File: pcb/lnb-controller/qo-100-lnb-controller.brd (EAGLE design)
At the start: 60 x 75 mm, 71 parts, among them CON1 2EDG-2P, Q1 AO3401, U1 LT8636, U2 ADP7142AUJZ-3.3, U3 DSC1201DE3-25M00000, U4 DSB321SDA, U5 MXT573ABC25M0000

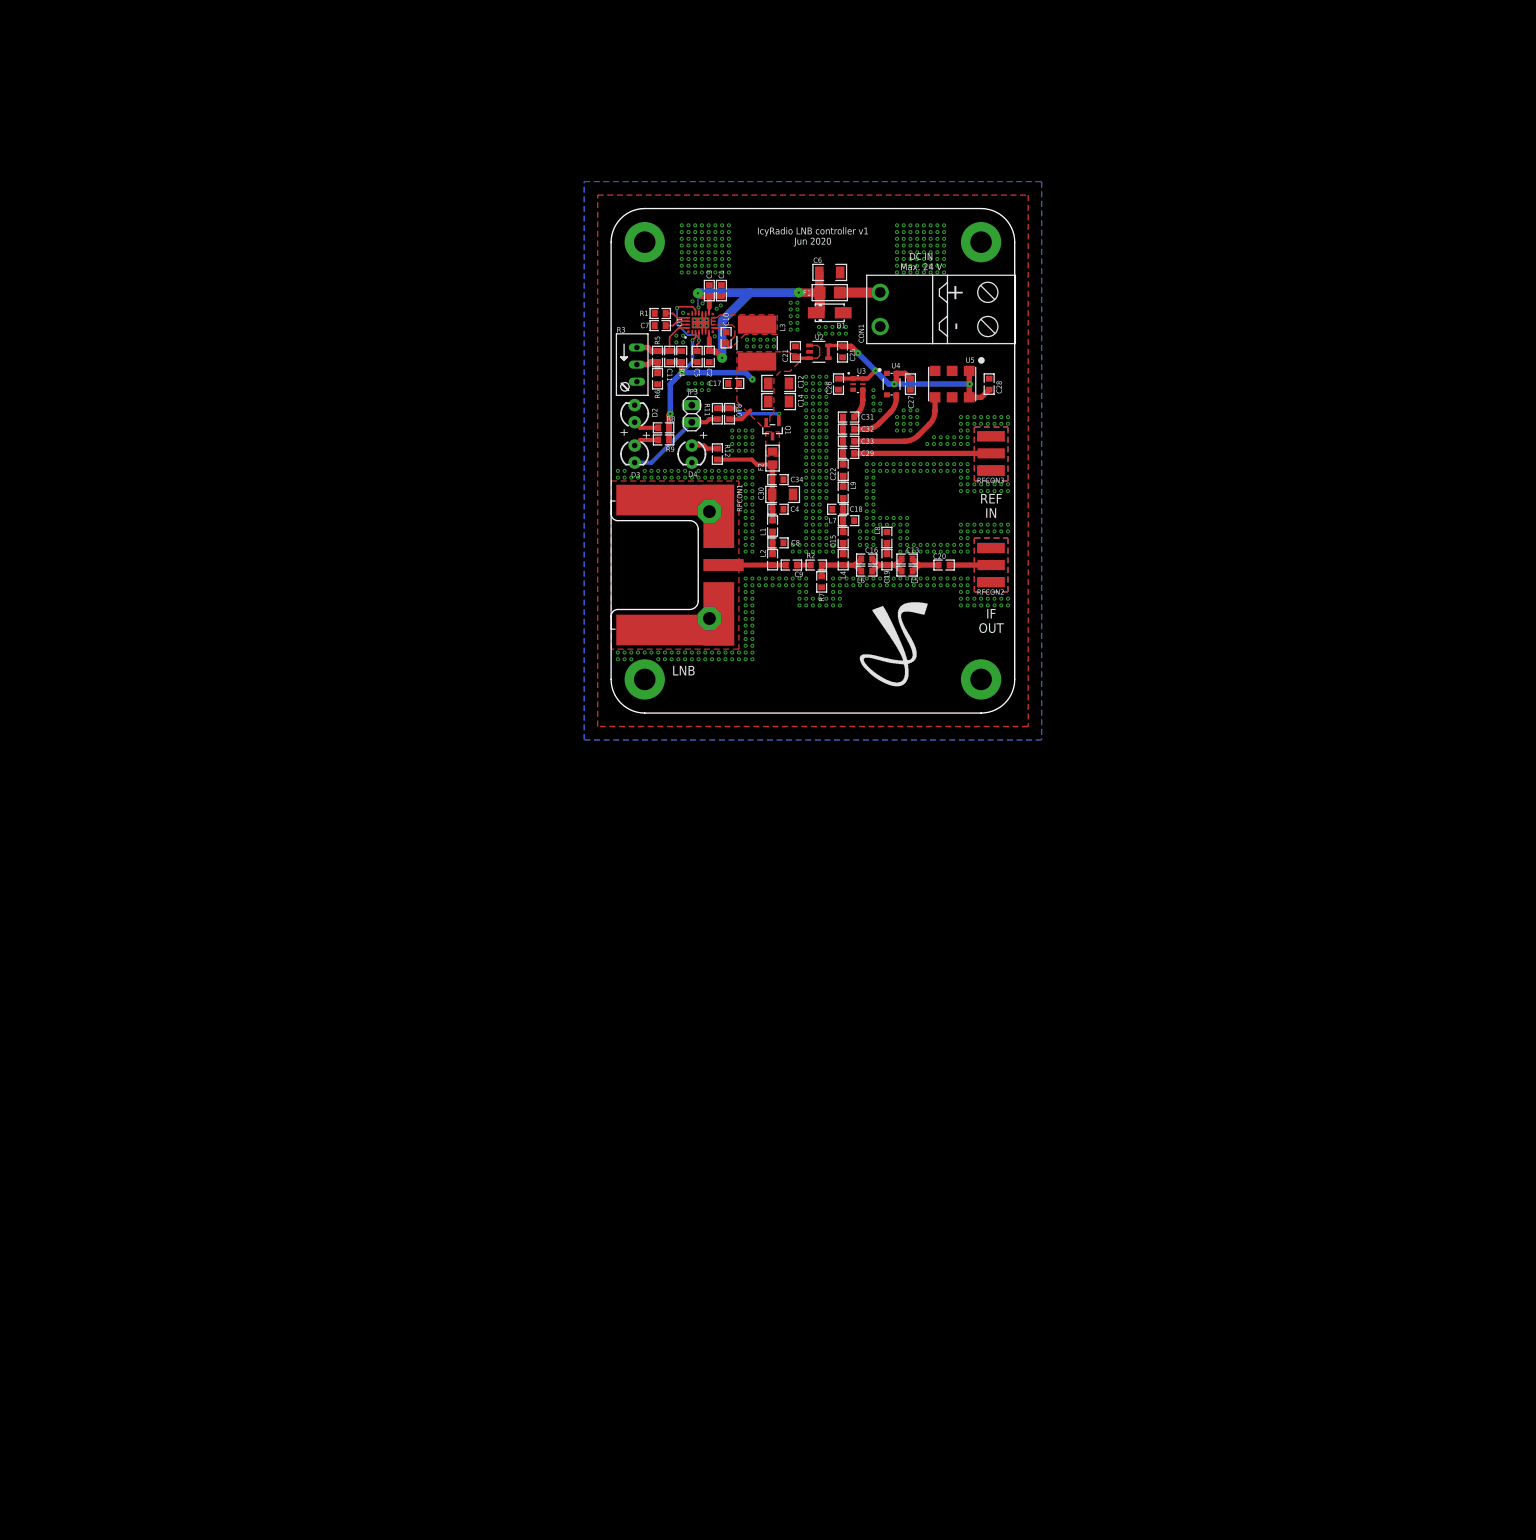
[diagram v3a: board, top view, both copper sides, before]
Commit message: Re-design LNB controller
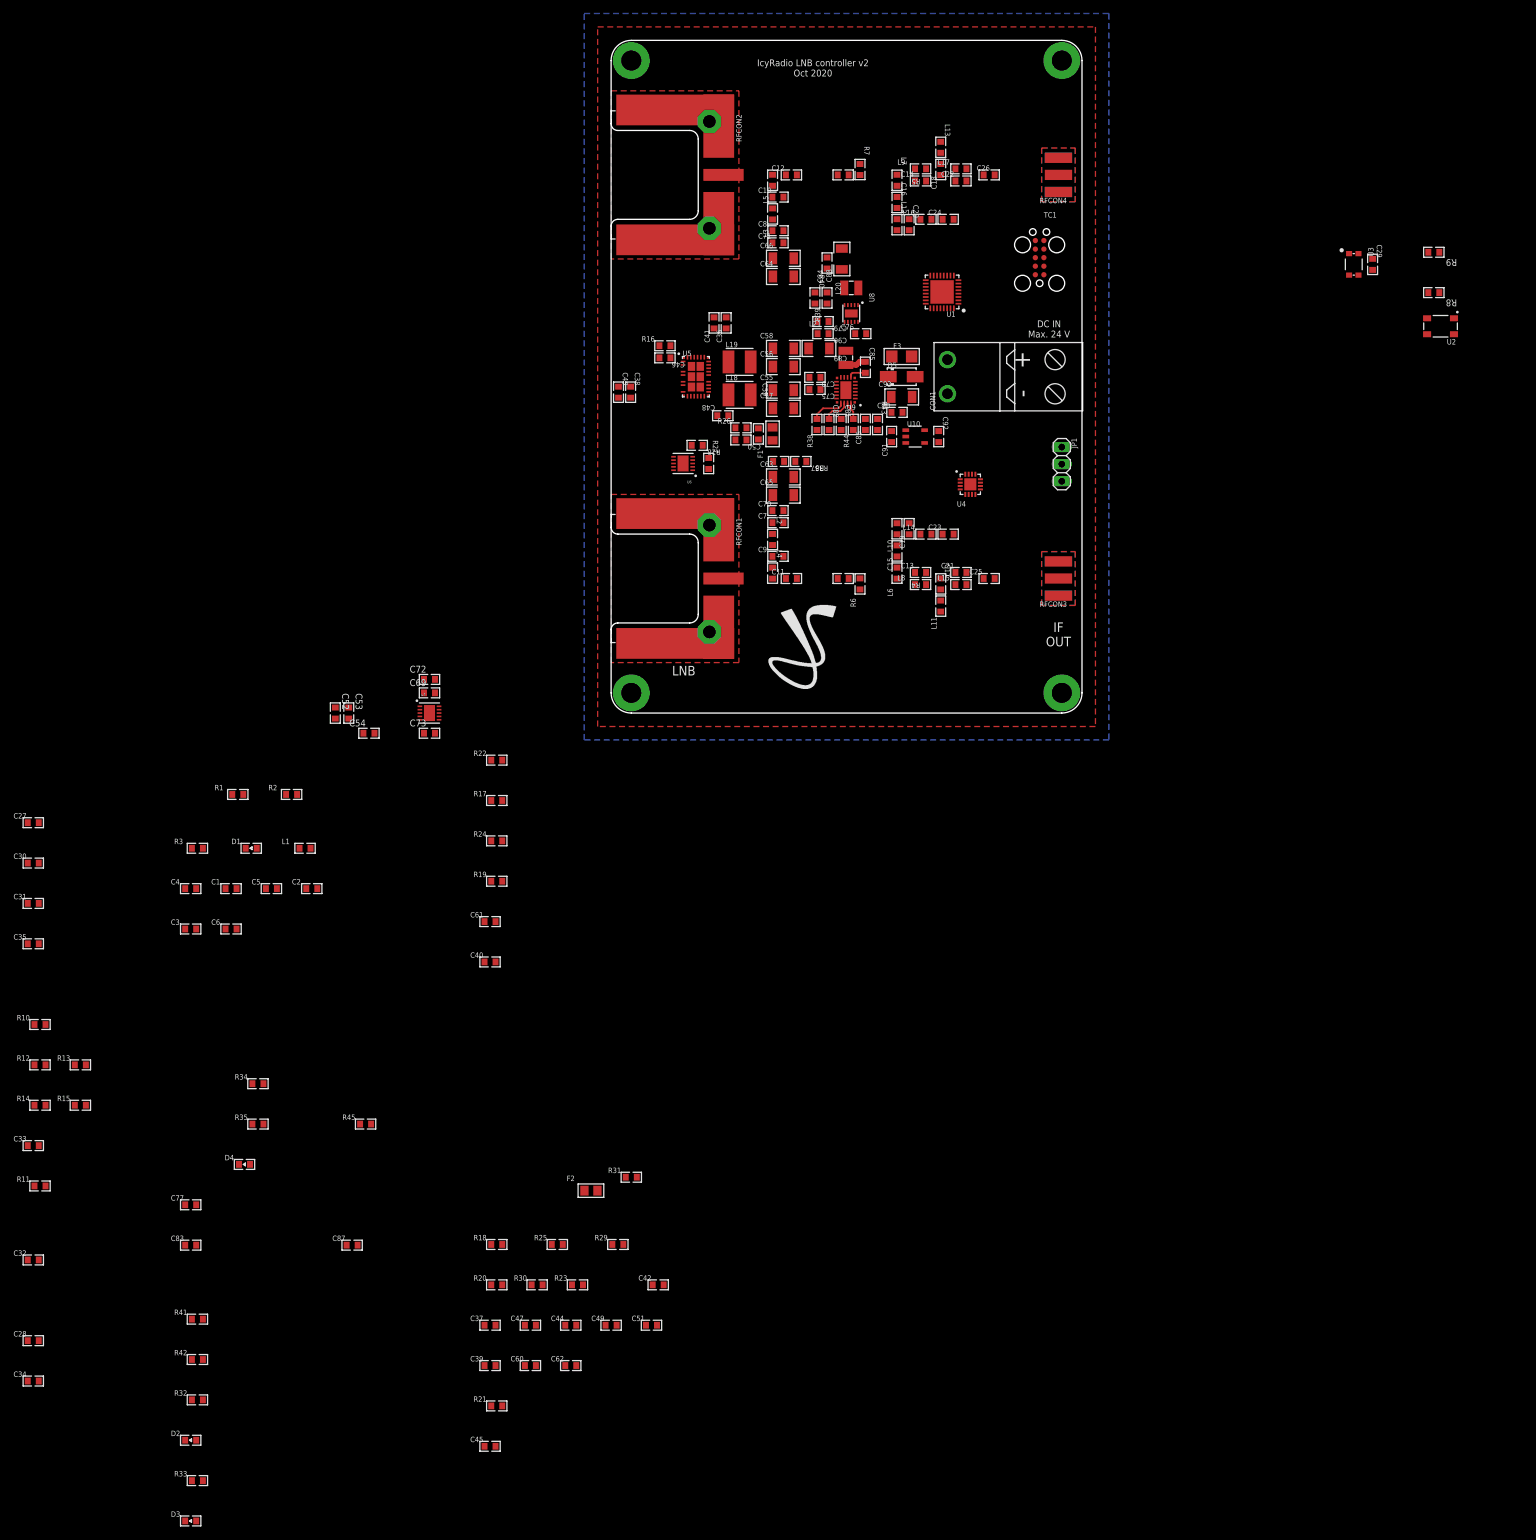
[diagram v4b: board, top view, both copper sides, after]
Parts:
- removed JP3: PINHD-1X2, Pin Header:1X02
- removed Q1: AO3401, Alpha Omega:SOT23
- added C23, C24: 100pF, Capacitor:CAP0603
- added C35, C48, C49, C53, C59, C60, C61, C62, C70, C71, C72, C84, C85, C90: 100nF, Capacitor:CAP0603
- added C36, C37, C75, C76: 4.7uF, Capacitor:CAP0603
- added C38, C39, C40, C41, C42, C54, C73, C78, C80, C81, C91: 1uF, Capacitor:CAP0603
- added C43, C44: DNP, Capacitor:CAP0603
- added C45, C77, C79, C83, C87: 470pF, Capacitor:CAP0603
- added C46, C47, C82: 10nF, Capacitor:CAP0603
- added C50, C51: 4.7pF, Capacitor:CAP0603
- added C52, C69, C92: 10uF, Capacitor:CAP0603
- added C55, C56, C57, C58, C63, C64, C65, C66: 22uF, Capacitor:CAP1206
- added C86: 10pF, Capacitor:CAP0603
- added C88, C89: 100uF, Capacitor:CAP1206
- added C93: 10uF, Capacitor:CAP1206
- added D5: SMAJ24A, TVS:DO214AC
- added F3: 2.6A Hold, PTC Fuses:1206
- added JP1: PINHD-1X3, Pin Header:1X03
- added L10, L12: 43nH, Inductor:IND0603
- added L11, L13: 330nH, Inductor:IND0603
- added L14, L16: 470nH, Inductor:IND0603
- added L15, L17: 120nH, Inductor:IND0603
- added L18, L19: 4.7uH, Inductor:IND0404
- added L20: 2.2uH, Inductor:IND2520
- added L21: 4.7uH, Inductor:IND2520
- added R13, R14, R15, R19, R20: 0 Ohms, Resistor:RES0603
- added R16: 15K Ohms, Resistor:RES0603
- added R17, R18, R24, R25, R34: 100K Ohms, Resistor:RES0603
- added R21: 1K Ohms, Resistor:RES0603
- added R22, R23, R27, R30: DNP, Resistor:RES0603
- added R26, R29, R43: 1M Ohms, Resistor:RES0603
- added R28, R31: 40.2K Ohms, Resistor:RES0603
- added R32, R33: 2.5K Ohms, Resistor:RES0603
- added R35: 10K Ohms, Resistor:RES0603
- added R36, R41: 90.9K Ohms, Resistor:RES0603
- added R37, R42: 12K Ohms, Resistor:RES0603
- added R38: 41.2K Ohms, Resistor:RES0603
- added R39: 309K Ohms, Resistor:RES0603
- added R40: 71.5K Ohms, Resistor:RES0603
- added R44: 226K Ohms, Resistor:RES0603
- added R45: 510 Ohms, Resistor:RES0603
- added RFCON4: RFCON-SMA-EDGE, RF Connector:SMA-EDGE
- added TC1: TC2050-IDC, TagConnect:TC2050-IDC
- added U10: ADP7142AUJZ-3.3, Analog Devices:SOT23-5
- added U6, U7: AD5272-100, Analog Devices:DFN10
- added U8: MIC23155, Microchip:DFN10
- added U9: LT8636, Analog Devices:QFN20_ASYM_CORNER
- C1: value 4.7uF -> 100nF
- C10, C17, C9: value 100nF -> 100pF
- C11: value 10pF -> 100nF
- C12, C30: value 22uF -> 100nF; device Capacitor:CAP1206 -> Capacitor:CAP0603
- C14: value 22uF -> 330pF; device Capacitor:CAP1206 -> Capacitor:CAP0603
- C16: value 330pF -> 100pF
- C18: value 1nF -> 100pF
- C19: value 100pF -> 1nF
- C2, C3: value 1uF -> 100nF
- C20: value 68pF -> 1nF
- C21: value 1uF -> 330pF
- C22: value 100pF -> 330pF
- C25: value 10uF -> 68pF
- C26: value 100nF -> 68pF
- C29, C31: value DNP -> 100nF
- C32: value DNP -> 15pF
- C33, C34: value 100nF -> 10pF
- C4: value 100nF -> 4.7uF
- C6: value 10uF -> 100nF; device Capacitor:CAP1206 -> Capacitor:CAP0603
- C7: value 10nF -> 100nF
- D1: value SMAJ24A -> LED0603; device TVS:DO214AC -> LED:0603
- D2, D3, D4: value LEDTH3MM -> LED0603; device LED:LED_3MM -> LED:0603
- F1: value 2.6A Hold -> (none); device PTC Fuses:1206 -> PTC Fuses:0805
- L1: value 470nH -> 4.7uH
- L3: value 4.7uH -> 470nH; device Inductor:IND0606 -> Inductor:IND0603
- L5, L6: value 120nH -> 470nH
- L7: value 43nH -> 470nH
- L8: value 330nH -> 120nH
- L9: value 470nH -> 120nH
- R1: value 41.2K Ohms -> 10K Ohms
- R10: value 10K Ohms -> 100K Ohms
- R12: value 2.5K Ohms -> 0 Ohms
- R2: value 43.2 Ohms -> 10K Ohms
- R3: value 100K Ohms -> 330 Ohms; device Potentiometer:TRIMMER -> Resistor:RES0603
- R4: value 1M Ohms -> 43.2 Ohms
- R5: value DNP -> 43.2 Ohms
- R6: value 47K Ohms -> 86.6 Ohms
- R8: value 2.5K Ohms -> 10K Ohms
- R9: value 2.5K Ohms -> 8.4K Ohms
- RFCON2: value RFCON-SMA-EDGE -> RFCON-F-EDGE; device RF Connector:SMA-EDGE -> RF Connector:F-EDGE
- U1: value LT8636 -> EFM32PG1B200F256GM32; device Analog Devices:QFN20_ASYM_CORNER -> EFM32:QFN32_0.5P_JPG
- U2: value ADP7142AUJZ-3.3 -> IQXT-210-3; device Analog Devices:SOT23-5 -> Crystal:IQXT-210-23
- U3: value DSC1201DE3-25M00000 -> DSB321SDA; device Microchip:VDFN6 -> Crystal:TCXO-3225
- U4: value DSB321SDA -> SI5351C-B-GM1; device Crystal:TCXO-3225 -> Silicon Labs:QFN16
- U5: value MXT573ABC25M0000 -> LT8650S-1; device Microchip:LGA6 -> Analog Devices:QFN28_ASYM_CORNER
- moved C28 201.0 mm to (-85.9, -93.3), turned to 0 degrees
- moved C34 173.8 mm to (-85.9, -99.3)
- moved C32 173.0 mm to (-85.9, -81.3), turned to 0 degrees
- moved D3 171.8 mm to (-62.5, -120.1), turned to 0 degrees
- moved D2 166.3 mm to (-62.5, -108.1), turned to 0 degrees
- moved C33 160.2 mm to (-85.9, -64.3), turned to 0 degrees
- moved R11 152.7 mm to (-84.9, -70.3), turned to 0 degrees
- moved C27 145.8 mm to (-85.9, -16.3), turned to 0 degrees
- moved C31 141.1 mm to (-85.9, -28.3), turned to 0 degrees
- moved R10 136.9 mm to (-84.9, -46.3), turned to 0 degrees
- moved R12 135.6 mm to (-84.9, -52.3), turned to 0 degrees
- moved C6 132.1 mm to (-56.5, -32.1)
- moved D4 124.8 mm to (-54.5, -67.1), turned to 0 degrees
- moved C30 124.1 mm to (-85.9, -22.3)
- moved C3 122.3 mm to (-62.5, -32.1), turned to 0 degrees
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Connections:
- removed net 12V0: C11.1, C12.1, C14.1, C17.1, C21.1, L3.2, Q1.2, R10.2, R4.2, R8.2, R9.2, U1.2, U2.1, U2.3
- removed net 12V0_BST: C10.2, U1.7
- removed net 12V0_FB: C11.2, R3.E, R4.1, R5.2, U1.19, U1.20
- removed net 12V0_INTVCC: C5.1, U1.15, U1.3
- removed net 12V0_RT: R1.2, U1.17
- removed net 12V0_SS: C7.1, U1.18
- removed net 12V0_SW: C10.1, L3.1, U1.10, U1.8, U1.9
- removed net LNB_BIAS: C30.1, C34.1, C4.1, F2.1, L1.1, R12.2
- removed net LNB_REF: C22.2, C29.2, C31.2, C32.2, C33.2
- removed net N$2: D3.K, JP3.1, R11.1
- removed net N$5: D3.A, R9.1
- new net !REF_SYNTH_OE: R10.1, U4.3
- new net !RESET: R1.1, TC1.10, U1.8
- new net 1V8: C4.1, L1.1, U1.28
- new net 3V1: R10.2
- new net 3V3_FB: R39.1, R40.2, U8.4
- new net 3V3_REF_CLEAN: C28.1, C29.1, C30.1, C31.1, C35.1, C92.1, R8.2, U10.4, U10.5, U2.4, U3.4, U4.11, U4.14, U4.8, U4.9
- new net 3V3_SOFTSTART: C79.1, U8.6
- new net 3V3_SW: L20.1, U8.1
- new net 5V0: C76.1, C86.1, C89.1, C90.1, C91.1, L21.2, R43.2, R45.2, U10.1, U10.3, U8.2, U8.8, U8.9, U9.2
- new net 5V0_BST: C85.2, U9.7
- new net 5V0_FB: C86.2, R43.1, R44.2, U9.19, U9.20
- new net 5V0_INTVCC: C81.1, U9.15, U9.3
- new net 5V0_RT: R38.2, U9.17
- new net 5V0_SS: C82.1, U9.18
- new net 5V0_SW: C85.1, L21.1, U9.10, U9.8, U9.9
- new net BIAS_REG_TEMP: C45.1, R21.1
- new net CLK_MNGR_CLK0: R12.2, U4.10
- new net CLK_MNGR_CLK1: R14.2, U4.7
- new net CLK_MNGR_CLK2: R13.2, U4.13
- new net CLK_MNGR_CLK3: R15.2, U4.12
- new net I2C_SCL: U4.4, U6.9, U7.9
- new net I2C_SDA: U4.5, U6.8, U7.8
- new net LED: R3.2, U1.31
- new net LNB_BIAS_SEL: C6.1, JP1.2, R2.2, U1.32
- new net N$23: D3.A, R33.1
- new net N$24: C12.1, L5.2, RFCON2.SIGNAL
- new net N$25: D1.A, R3.1
- new net N$26: C12.2, R5.2
- new net N$27: C10.1, L3.2, L5.1
- new net N$28: C24.1, L16.2
- new net N$29: C16.1, L7.2
- new net N$30: C16.2, C20.1, L12.1, L16.1
- new net N$31: C14.1, L7.1, L9.1, R5.1, R7.2
- new net N$32: C14.2, C18.1, C22.1, L17.1, L9.2
- new net N$33: C26.2, RFCON4.SIG
- new net N$34: C18.2, L13.2
- new net N$35: C22.2, C26.1, L17.2
- new net N$36: C34.2, U4.1
- new net N$37: C32.1, U2.3, U4.6
- new net N$39: C54.1, U6.5
- new net N$40: C73.1, U7.5
- new net REF1: C23.2, R12.1
- new net REF2: C24.2, R14.1
- new net REF_XO_VC: R8.1, R9.2, U2.1
- new net SWCLK: TC1.4, U1.1
- new net SWDIO: TC1.2, U1.2
- new net SWO: TC1.6, U1.3
- new net VBIAS1: C63.1, C65.1, C7.1, C70.1, F1.1, L2.1, R32.2, R36.2
- new net VBIAS1_BST: C48.2, U5.15
- new net VBIAS1_EN: R17.2, U5.9
- new net VBIAS1_FB: C50.2, R26.1, R27.2, U5.27, U6.2
- new net VBIAS1_FB_DIV: R27.1, R28.2, U6.3
- new net VBIAS1_PG: R24.1, U5.12
- new net VBIAS1_SS: C46.1, U5.26
- new net VBIAS1_SW: C48.1, L18.1, U5.16, U5.17
- new net VBIAS1_UNFUSED: C50.1, C55.1, C57.1, C59.1, C61.1, F1.2, L18.2, R26.2, U5.22
- new net VBIAS1_VC: R19.1, R22.2, U5.28
- new net VBIAS1_VSENSE: C83.1, R36.1, R37.2, U1.19
- new net VBIAS2: C64.1, C66.1, C71.1, C8.1, F2.1, L3.1, R33.2, R41.2
- new net VBIAS2_BST: C49.2, U5.20
- new net VBIAS2_EN: R18.2, U5.8
- new net VBIAS2_FB: C51.2, R29.1, R30.2, U5.24, U7.2
- new net VBIAS2_FB_DIV: R30.1, R31.2, U7.3
- new net VBIAS2_PG: R25.1, U5.11
- new net VBIAS2_SS: C47.1, U5.25
- new net VBIAS2_SW: C49.1, L19.1, U5.18, U5.19
- new net VBIAS2_UNFUSED: C51.1, C56.1, C58.1, C60.1, C62.1, F2.2, L19.2, R29.2
- new net VBIAS2_VC: R20.1, R23.2, U5.23
- new net VBIAS2_VSENSE: C87.1, R41.1, R42.2, U1.20
- new net VBIAS_VCC: C40.1, R19.2, R20.2, U5.13, U5.21
- new net VIN_VSENSE: C77.1, R34.1, R35.2, U1.21
- net 3V3: now also C1.1, C2.1, C3.1, C52.1, C53.1, C69.1, C72.1, C84.1, C88.1, JP1.1, L20.2, R1.2, R24.2, R25.2, R39.2, TC1.1, U1.22, U1.27, U1.30, U1.5, U4.16, U6.1, U6.10, U6.7, U7.1, U7.7, U8.3; no longer C25.1, C26.1, C28.1, U2.4, U2.5, U3.1, U3.6, U4.4, U5.1, U5.6
- net GND: now also C10.2, C19.2, C20.2, C29.2, C31.2, C32.2, C33.2, C35.2, C36.2, C37.2, C38.2, C39.2, C40.2, C41.2, C42.2, C43.2, C44.2, C45.2, C46.2, C47.2, C52.2, C53.2, C54.2, C55.2, C56.2, C57.2, C58.2, C59.2, C60.2, C61.2, C62.2, C63.2, C64.2, C65.2, C66.2, C69.2, C70.2, C71.2, C72.2, C73.2, C75.2, C76.2, C77.2, C78.2, C79.2, C80.2, C81.2, C82.2, C83.2, C84.2, C87.2, C88.2, C89.2, C9.2, C90.2, C91.2, C92.2, C93.2, D1.C, D2.C, D3.C, D4.C, D5.A, JP1.3, L10.2, L11.1, L12.2, L13.1, R11.1, R16.1, R17.1, R18.1, R2.1, R28.1, R31.1, R35.1, R37.1, R38.1, R40.1, R42.1, R44.1, R9.1, RFCON2.GND@4, RFCON2.GND@5, RFCON4.GND@0, RFCON4.GND@1, RFCON4.GND@2, RFCON4.GND@3, TC1.3, U1.25, U1.33, U10.2, U3.1, U3.2, U4.15, U4.17, U5.2, U5.29, U5.30, U5.31, U5.32, U5.33, U5.34, U5.35, U5.36, U5.37, U5.38, U5.7, U6.11, U6.4, U6.6, U7.10, U7.11, U7.4, U7.6, U8.10, U8.11, U8.7, U9.12, U9.13, U9.21, U9.4, U9.5, U9.M1, U9.M2, U9.M3, U9.M4; no longer C12.2, C14.2, C17.2, C18.2, C21.2, C25.2, C26.2, C34.2, D1.A, D2.K, D4.K, JP3.2, L7.2, L8.1, R1.1, U1.12, U1.13, U1.21, U1.4, U1.5, U1.M1, U1.M2, U1.M3, U1.M4, U3.3, U4.1, U4.2, U5.3
- net N$1: now also C43.1, R22.1; no longer F2.2, Q1.3
- net N$10: now also C11.2, R4.2; no longer C9.2, R2.2
- net N$11: now also D2.A, R32.1; no longer D4.A, R12.1
- net N$12: now also C23.1, L14.2; no longer C22.1, L9.2
- net N$13: now also C9.1, L2.2, L4.1; no longer C8.1, L1.2, L2.1
- net N$14: now also L6.2; no longer L4.2
- net N$149: now also D4.A, R45.1; no longer D2.A, R8.1
- net N$15: now also C19.1, L10.1, L14.1; no longer C18.1, L7.1, L9.1
- net N$16: now also C21.2, C25.1, L15.2; no longer C13.2, C20.1, L5.2
- net N$17: now also C13.1, L8.1, R4.1, R6.2; no longer C16.1, L4.1, R2.1, R7.2
- net N$18: now also C13.2, C17.1, C21.1, L15.1, L8.2; no longer C13.1, C16.2, C19.1, L5.1, L6.2
- net N$19: now also F3.2; no longer F1.2
- net N$20: now also C25.2, RFCON3.SIG; no longer C20.2, RFCON2.SIG
- net N$21: now also L1.2, U1.26; no longer R3.S, R5.1, R6.2
- net N$22: now also C17.2, L11.2; no longer C19.2, L8.2
- net N$3: now also R16.2, U5.1; no longer Q1.1, R10.1, R11.2
- net N$4: now also C44.1, R23.1; no longer C29.1, RFCON3.SIG
- net N$6: now also C5.1, U1.29; no longer C31.1, U3.4
- net N$7: now also C33.1, C34.1, R11.2, U3.3; no longer C32.1, U4.3
- net N$8: now also R21.2, U5.10; no longer C33.1, U5.4
- net N$9: now also C11.1, L4.2; no longer C9.1, L2.2
- net VIN: now also C36.1, C37.1, C38.1, C39.1, C41.1, C42.1, C75.1, C78.1, C80.1, C93.1, D5.C, F3.1, R34.2, U5.3, U5.4, U5.5, U5.6, U9.11, U9.14, U9.6; no longer C1.1, C2.1, C3.1, C6.1, D1.C, F1.1, U1.11, U1.14, U1.6
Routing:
- net VIN: track 50.3 -> 0.00 mm, vias 4 -> 0
- net 3V3: track 42.8 -> 0.00 mm, vias 4 -> 0
- net 12V0: track 42.2 -> 0.00 mm, vias 4 -> 0
- net N$4: track 20.4 -> 0.00 mm
- net LNB_BIAS: track 16.9 -> 0.00 mm
- net N$8: track 16.2 -> 0.00 mm
- net N$2: track 15.0 -> 0.00 mm
- net 12V0_FB: track 13.8 -> 0.00 mm
- net 12V0_INTVCC: track 13.3 -> 0.00 mm, vias 2 -> 0
- net N$3: track 10.8 -> 0.00 mm, vias 2 -> 0
- net N$9: track 9.30 -> 0.00 mm
- net N$17: track 9.21 -> 0.00 mm
- net N$7: track 9.01 -> 0.00 mm
- net N$18: track 7.70 -> 0.00 mm
- net LNB_REF: track 7.09 -> 0.00 mm
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- removed copper zone on layer 1, net 12V0
- removed copper zone on layer 1, net 12V0_SW
- removed copper zone on layer 1, net N$1
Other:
- board size 60 x 75 mm -> 70 x 100 mm
- board text added: "IcyRadio LNB controller v2 Oct 2020"
- board text removed: "IcyRadio LNB controller v1 Jun 2020"
- board text removed: "REF IN"

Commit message: LNB controller v2 work
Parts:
- removed C26: 68pF, Capacitor:CAP0603
- removed C85, C90: 100nF, Capacitor:CAP0603
- removed C86: 10pF, Capacitor:CAP0603
- removed C87: 470pF, Capacitor:CAP0603
- removed C88, C89: 100uF, Capacitor:CAP1206
- removed C91: 1uF, Capacitor:CAP0603
- removed C92: 10uF, Capacitor:CAP0603
- removed C93: 10uF, Capacitor:CAP1206
- removed R43: 1M Ohms, Resistor:RES0603
- removed R44: 226K Ohms, Resistor:RES0603
- removed R45: 510 Ohms, Resistor:RES0603
- added C67, C68: 470pF, Capacitor:CAP0603
- added RFCON5: RFCON-U.FL, RF Connector:U.FL
- C10: value 100pF -> 100nF
- C12: value 100nF -> 330pF
- C14, C22: value 330pF -> 100pF
- C18: value 100pF -> 1nF
- C20: value 1nF -> 330pF
- C24: value 100pF -> 68pF
- C3: value 100nF -> 4.7uF
- C31: value 100nF -> 15pF
- C32: value 15pF -> 10pF
- C34: value 10pF -> 100nF
- C35, C70, C71: value 100nF -> 1uF
- C36, C37: value 4.7uF -> 10nF
- C38, C73: value 1uF -> 470pF
- C39, C40, C5, C54, C80: value 1uF -> 100nF
- C4: value 4.7uF -> 1uF
- C41: value 1uF -> 4.7uF
- C42: value 1uF -> 4.7pF
- C43: value DNP -> 4.7pF
- C44: value DNP -> 1uF
- C45: value 470pF -> 22uF; device Capacitor:CAP0603 -> Capacitor:CAP1206
- C46, C47: value 10nF -> 22uF; device Capacitor:CAP0603 -> Capacitor:CAP1206
- C48, C59: value 100nF -> 22uF; device Capacitor:CAP0603 -> Capacitor:CAP1206
- C50, C51: value 4.7pF -> 100nF
- C55, C64: value 22uF -> 1uF; device Capacitor:CAP1206 -> Capacitor:CAP0603
- C62: value 100nF -> 10uF
- C63: value 22uF -> 100nF; device Capacitor:CAP1206 -> Capacitor:CAP0603
- C65, C66: value 22uF -> 4.7uF; device Capacitor:CAP1206 -> Capacitor:CAP0603
- C69: value 10uF -> 1uF
- C72: value 100nF -> 10nF
- C75: value 4.7uF -> 100nF
- C76: value 4.7uF -> 10pF
- C78: value 1uF -> 100uF; device Capacitor:CAP0603 -> Capacitor:CAP1206
- C79: value 470pF -> 100uF; device Capacitor:CAP0603 -> Capacitor:CAP1206
- C8: value 100nF -> 100pF
- C82: value 10nF -> 10uF
- C83: value 470pF -> 10uF; device Capacitor:CAP0603 -> Capacitor:CAP1206
- R10: value 100K Ohms -> 10K Ohms
- R11: value 10K Ohms -> 8.4K Ohms
- R12, R20: value 0 Ohms -> 100K Ohms
- R13: value 0 Ohms -> 10K Ohms
- R16: value 15K Ohms -> 0 Ohms
- R19: value 0 Ohms -> 15K Ohms
- R2: value 10K Ohms -> 1K Ohms
- R21: value 1K Ohms -> 100K Ohms
- R22: value DNP -> 1K Ohms
- R23: value DNP -> 1M Ohms
- R24: value 100K Ohms -> DNP
- R25: value 100K Ohms -> 40.2K Ohms
- R29: value 1M Ohms -> 2.5K Ohms
- R3: value 330 Ohms -> 1K Ohms
- R30: value DNP -> 2.5K Ohms
- R31: value 40.2K Ohms -> 100K Ohms
- R32: value 2.5K Ohms -> 10K Ohms
- R33: value 2.5K Ohms -> 90.9K Ohms
- R34: value 100K Ohms -> 12K Ohms
- R35: value 10K Ohms -> 41.2K Ohms
- R36: value 90.9K Ohms -> 309K Ohms
- R37: value 12K Ohms -> 71.5K Ohms
- R38: value 41.2K Ohms -> 90.9K Ohms
- R39: value 309K Ohms -> 12K Ohms
- R4: value 43.2 Ohms -> 10K Ohms
- R40: value 71.5K Ohms -> 1M Ohms
- R41: value 90.9K Ohms -> 226K Ohms
- R42: value 12K Ohms -> 510 Ohms
- R5: value 43.2 Ohms -> 330 Ohms
- R6, R7: value 86.6 Ohms -> 43.2 Ohms
- R8: value 10K Ohms -> 86.6 Ohms
- R9: value 8.4K Ohms -> 86.6 Ohms
- moved R11 253.7 mm to (130.6, 63.5), turned to 180 degrees
- moved R10 241.2 mm to (130.8, 61.6), turned to 180 degrees
- moved C31 232.8 mm to (133.6, 49.2)
- moved C27 230.1 mm to (133.9, 51.7)
- moved D3 201.3 mm to (20.2, 63.4), turned to 90 degrees
- moved C28 195.6 mm to (58.0, 39.2), turned to 270 degrees
- moved R32 190.8 mm to (43.2, 57.4)
- moved C34 189.5 mm to (52.5, 30.2), turned to 270 degrees
- moved C32 184.4 mm to (51.2, 42.0), turned to 90 degrees
- moved C33 174.5 mm to (54.6, 39.2)
- moved R33 174.4 mm to (24.8, 37.4), turned to 180 degrees
- moved R12 174.3 mm to (61.3, 42.6)
- moved C77 173.4 mm to (42.3, 65.0), turned to 180 degrees
- moved R42 168.1 mm to (37.8, 39.5), turned to 90 degrees
- moved R15 166.7 mm to (59.5, 34.6), turned to 180 degrees
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- renumbered C84 to C74
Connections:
- removed net 3V1: R10.2
- removed net CLK_MNGR_CLK0: R12.2, U4.10
- removed net CLK_MNGR_CLK1: R14.2, U4.7
- removed net CLK_MNGR_CLK2: R13.2, U4.13
- removed net CLK_MNGR_CLK3: R15.2, U4.12
- removed net N$4: C44.1, R23.1
- removed net VBIAS1_VC: R19.1, R22.2, U5.28
- removed net VBIAS2_VC: R20.1, R23.2, U5.23
- new net N$2: R15.2, U4.13
- new net N$41: R16.1, RFCON5.P$3
- new net N$5: R14.2, U4.10
- net !REF_SYNTH_OE: now also R12.1, U1.10; no longer R10.1
- net 1V8: now also C3.1; no longer C4.1
- net 3V3: now also C54.1, C62.1, C63.1, C78.1, R12.2, R2.2, R20.2, R21.2, R3.2, R36.2; no longer C27.1, C3.1, C53.1, C69.1, C72.1, C88.1, R24.2, R25.2, R39.2, U4.16
- net 3V3_FB: now also R36.1, R37.2; no longer R39.1, R40.2
- net 3V3_REF_CLEAN: now also C27.1, C34.1, C82.1, R10.2, U4.16; no longer C31.1, C35.1, C92.1, R8.2
- net 3V3_SOFTSTART: now also C68.1; no longer C79.1
- net 5V0: now also C66.1, C79.1, C80.1, C81.1, R40.2, R42.2; no longer C86.1, C89.1, C90.1, C91.1, R43.2, R45.2
- net 5V0_BST: now also C75.2; no longer C85.2
- net 5V0_FB: now also C76.2, R40.1, R41.2; no longer C86.2, R43.1, R44.2
- net 5V0_INTVCC: now also C71.1; no longer C81.1
- net 5V0_RT: now also R35.2; no longer R38.2
- net 5V0_SS: now also C72.1; no longer C82.1
- net 5V0_SW: now also C75.1; no longer C85.1
- net BIAS_REG_TEMP: now also C38.1, R22.1, U1.19; no longer C45.1, R21.1
- net GND: now also C18.2, C34.2, C48.2, C49.2, C50.2, C51.2, C67.2, C68.2, R13.1, R19.1, R25.1, R32.1, R34.1, R39.1, R4.1, R41.1, R8.1, RFCON5.P$1, RFCON5.P$2; no longer C10.2, C20.2, C33.2, C39.2, C40.2, C42.2, C43.2, C75.2, C76.2, C87.2, C88.2, C89.2, C90.2, C91.2, C92.2, C93.2, R16.1, R2.1, R31.1, R38.1, R40.1, R42.1, R44.1, R6.1, R7.1
- net I2C_SCL: now also R3.1, U1.32
- net I2C_SDA: now also R2.1, U1.31
- net LED: now also R5.2, U1.4; no longer R3.2, U1.31
- net LNB_BIAS_SEL: now also C5.1, R4.2, U1.11; no longer C6.1, R2.2, U1.32
- net N$1: now also R16.2, U4.12; no longer C43.1, R22.1
- net N$10: now also C10.2, R6.2; no longer C11.2, R4.2
- net N$11: now also R29.1; no longer R32.1
- net N$12: now also C22.1; no longer C23.1
- net N$13: now also C8.1; no longer C9.1
- net N$14: now also C14.1; no longer C15.1
- net N$149: now also R42.1; no longer R45.1
- net N$15: now also C14.2, C18.1; no longer C15.2, C19.1
- net N$16: now also C20.2, C24.1; no longer C21.2, C25.1
- net N$17: now also C12.1, R6.1, R8.2; no longer C13.1, R4.1, R6.2
- net N$18: now also C12.2, C16.1, C20.1; no longer C13.2, C17.1, C21.1
- net N$20: now also C24.2; no longer C25.2
- net N$22: now also C16.2; no longer C17.2
- net N$23: now also R30.1; no longer R33.1
- net N$24: now also C11.1; no longer C12.1
- net N$25: now also R5.1; no longer R3.1
- net N$26: now also C11.2, R7.2; no longer C12.2, R5.2
- net N$27: now also C9.1; no longer C10.1
- net N$28: now also C23.1; no longer C24.1
- net N$29: now also C15.1; no longer C16.1
- net N$3: now also R19.2; no longer R16.2
- net N$30: now also C15.2, C19.1; no longer C16.2, C20.1
- net N$31: now also C13.1, R7.1, R9.2; no longer C14.1, R5.1, R7.2
- net N$32: now also C13.2, C17.1, C21.1; no longer C14.2, C18.1, C22.1
- net N$33: now also C25.2; no longer C26.2
- net N$34: now also C17.2; no longer C18.2
- net N$35: now also C21.2, C25.1; no longer C22.2, C26.1
- net N$36: now also C33.2; no longer C34.2
- net N$37: now also C31.1; no longer C32.1
- net N$39: now also C55.1; no longer C54.1
- net N$40: now also C64.1; no longer C73.1
- net N$6: now also C4.1; no longer C5.1
- net N$7: now also C32.1, R13.2; no longer C34.1, R11.2
- net N$8: now also R22.2; no longer R21.2
- net N$9: now also C10.1; no longer C11.1
- net REF1: now also C22.2, R14.1; no longer C23.2, R12.1
- net REF2: now also C23.2, R15.1; no longer C24.2, R14.1
- net REF_XO_VC: now also R10.1, R11.2; no longer R8.1, R9.2
- net VBIAS1: now also C56.1, C58.1, C6.1, C60.1, R29.2, R33.2; no longer C63.1, C65.1, C7.1, C70.1, R32.2, R36.2
- net VBIAS1_BST: now also C39.2; no longer C48.2
- net VBIAS1_EN: now also U1.16
- net VBIAS1_FB: now also C42.2, R23.1, R24.2; no longer C50.2, R26.1, R27.2
- net VBIAS1_FB_DIV: now also R24.1, R25.2; no longer R27.1, R28.2
- net VBIAS1_PG: now also R20.1, U1.18; no longer R24.1
- net VBIAS1_SS: now also C36.1; no longer C46.1
- net VBIAS1_SW: now also C39.1; no longer C48.1
- net VBIAS1_UNFUSED: now also C42.1, C45.1, C47.1, C49.1, C51.1, R23.2; no longer C50.1, C55.1, C57.1, C59.1, C61.1, R26.2
- net VBIAS1_VSENSE: now also C73.1, R33.1, R34.2, U1.20; no longer C83.1, R36.1, R37.2, U1.19
- net VBIAS2: now also C57.1, C59.1, C61.1, C7.1, R30.2, R38.2; no longer C64.1, C66.1, C71.1, C8.1, R33.2, R41.2
- net VBIAS2_BST: now also C40.2; no longer C49.2
- net VBIAS2_EN: now also U1.15
- net VBIAS2_FB: now also C43.2, R26.1, R27.2; no longer C51.2, R29.1, R30.2
- net VBIAS2_FB_DIV: now also R27.1, R28.2; no longer R30.1, R31.2
- net VBIAS2_PG: now also R21.1, U1.17; no longer R25.1
- net VBIAS2_SS: now also C37.1; no longer C47.1
- net VBIAS2_SW: now also C40.1; no longer C49.1
- net VBIAS2_UNFUSED: now also C43.1, C46.1, C48.1, C50.1, C53.1, R26.2; no longer C51.1, C56.1, C58.1, C60.1, C62.1, R29.2
- net VBIAS2_VSENSE: now also C77.1, R38.1, R39.2, U1.21; no longer C87.1, R41.1, R42.2, U1.20
- net VBIAS_VCC: now also C35.1, U5.23, U5.28; no longer C40.1, R19.2, R20.2
- net VIN: now also C44.1, C65.1, C69.1, C70.1, C83.1, R31.2; no longer C36.1, C37.1, C38.1, C39.1, C42.1, C75.1, C78.1, C80.1, C93.1, R34.2
- net VIN_VSENSE: now also C67.1, R31.1, R32.2, U1.23; no longer C77.1, R34.1, R35.2, U1.21
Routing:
- net REF2: track 0.00 -> 62.8 mm, vias 0 -> 2
- net VIN: track 0.00 -> 48.0 mm, vias 0 -> 2
- net 3V3_REF_CLEAN: track 0.00 -> 45.7 mm, vias 0 -> 7
- net LNB_BIAS_SEL: track 0.00 -> 43.2 mm, vias 0 -> 4
- net !REF_SYNTH_OE: track 0.00 -> 41.9 mm, vias 0 -> 5
- net 3V3: track 0.00 -> 32.4 mm, vias 0 -> 5
- net I2C_SDA: track 0.00 -> 32.2 mm, vias 0 -> 4
- net I2C_SCL: track 0.00 -> 31.8 mm, vias 0 -> 4
- net VBIAS_VCC: track 0.00 -> 27.9 mm, vias 0 -> 3
- net VBIAS1_FB: track 0.00 -> 27.0 mm, vias 0 -> 3
- net VBIAS2: track 0.00 -> 16.1 mm
- net N$17: track 0.00 -> 15.7 mm
- net VBIAS1_PG: track 0.00 -> 15.7 mm, vias 0 -> 1
- net N$31: track 0.00 -> 15.7 mm
- net VBIAS1: track 0.00 -> 15.6 mm
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- added copper zone on layer 1, net VBIAS1_SW
- added copper zone on layer 1, net VBIAS1_UNFUSED
- added copper zone on layer 1, net VBIAS2_SW
- added copper zone on layer 1, net VBIAS2_UNFUSED
- added copper zone on layer 1, net VIN
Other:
- board text added: "0"
- board text added: "1"
- board text added: "IcyRadio LNB controller v2 Sep 2020"
- board text removed: "IcyRadio LNB controller v2 Oct 2020"

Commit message: LNB converter work
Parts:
- moved C71 5.17 mm to (30.3, 46.3), turned to 180 degrees
- moved C72 1.80 mm to (34.2, 42.9)
- moved R35 1.80 mm to (32.4, 42.9)
- moved L20 0.60 mm to (36.3, 63.2)
- moved C78 0.40 mm to (34.7, 67.5)
- moved C74 0.40 mm to (32.5, 66.9)
- moved R37 0.10 mm to (29.9, 60.9)
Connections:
- net 5V0: now also U5.22
- net VBIAS1_UNFUSED: no longer U5.22
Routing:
- net 5V0: track 11.6 -> 59.9 mm, vias 0 -> 7
- net VIN: track 48.0 -> 70.4 mm, vias 2 -> 4
- net 5V0_INTVCC: track 0.00 -> 11.6 mm, vias 0 -> 2
- net GND: track 3.83 -> 12.4 mm, vias 145 -> 157
- net 3V3_FB: track 0.00 -> 5.28 mm
- net 5V0_FB: track 3.68 -> 7.58 mm
- net 3V3: track 32.4 -> 35.2 mm
- net 3V3_SOFTSTART: track 0.00 -> 2.40 mm
- net VBIAS_VCC: track 27.9 -> 30.1 mm
- net 5V0_RT: track 5.20 -> 3.12 mm
- net VIN_VSENSE: track 0.00 -> 1.80 mm
- net VBIAS1_UNFUSED: track 3.59 -> 1.80 mm, vias 1 -> 0
- net 5V0_SS: track 4.02 -> 2.57 mm
- added copper zone on layer 1, net 3V3
- added copper zone on layer 1, net 3V3_SW
- added copper zone on layer 1, net 5V0
- added copper zone on layer 1, net 5V0_SW
